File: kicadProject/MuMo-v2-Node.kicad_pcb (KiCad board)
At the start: 2 copper layers, 52 x 50.3 mm, 79 parts, among them Q1 PJC7400, SW1 Reset, U1 MCP73123T-22SI/MF, U2 LoRa-E5, U3 CP2102N-Axx-xQFN24, U4 eInk_Display_1.54"200x200px, U5 BME680, U6 TSL25911, U7 BR24G512FVT-5AE2, U8 BR24G512FVT-5AE2

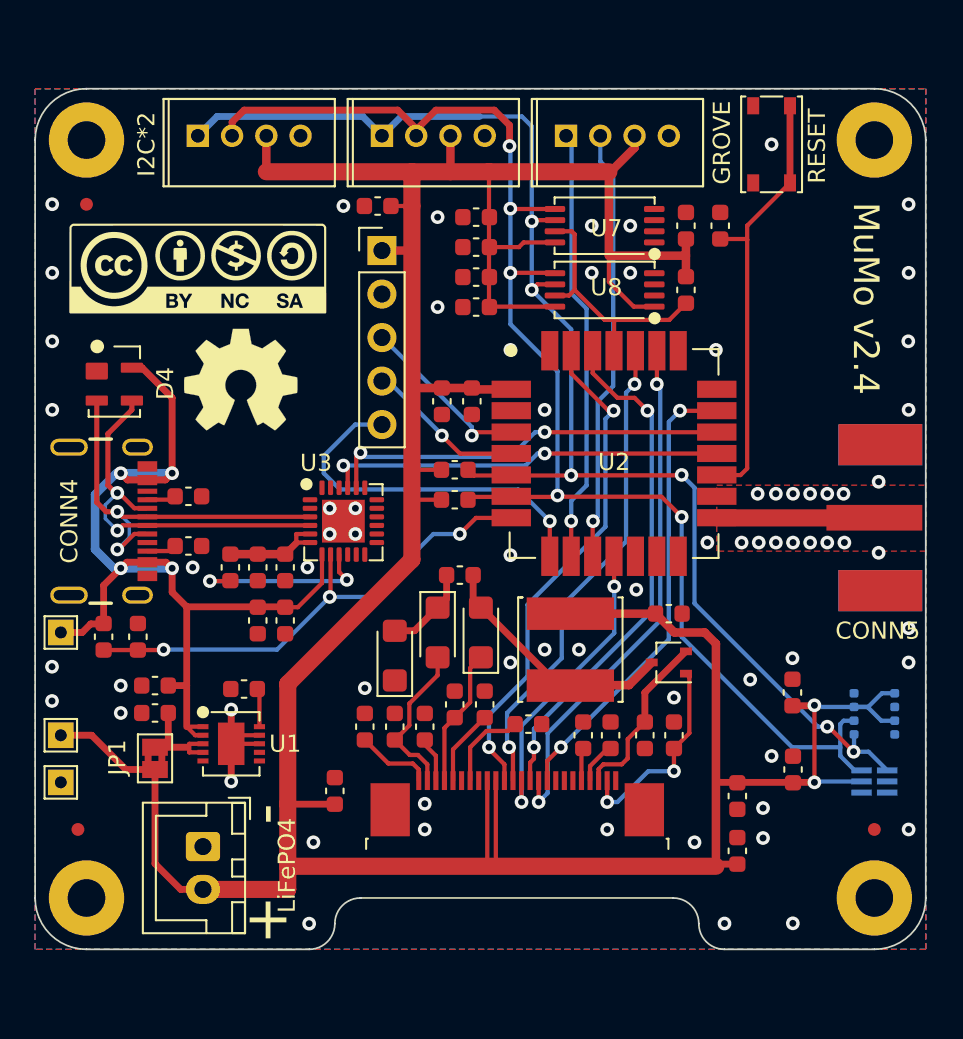
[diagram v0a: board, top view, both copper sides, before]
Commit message: add 3d model for enclosure
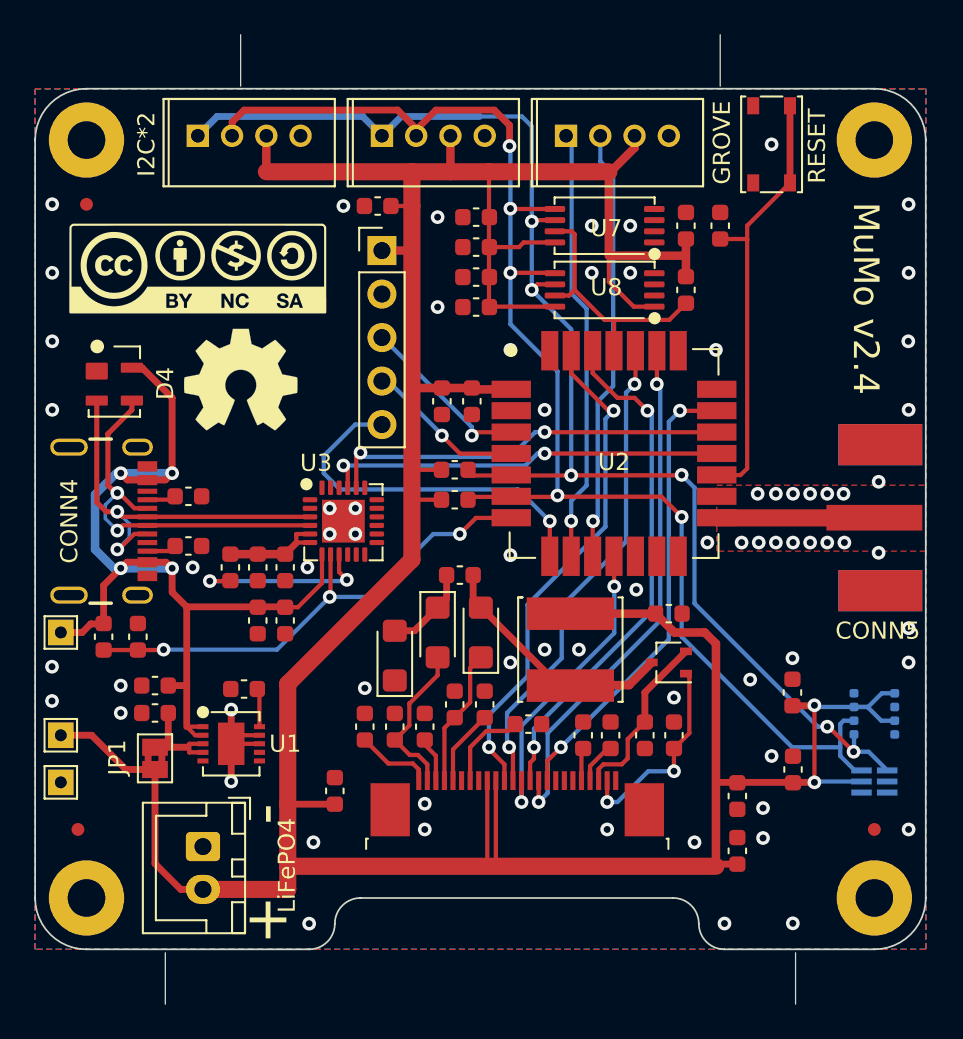
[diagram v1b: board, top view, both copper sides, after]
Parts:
- CONN2: value B2B-XH-A (LF)(SN) -> B2B-XH-A(LF)(SN)
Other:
- board size 52 x 50.3 mm -> 52 x 56.6 mm
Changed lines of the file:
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@@
     (property "DESCRIPTION" "JST XH 2pin THT Vertical")
     (property "MANUFACTURER" "JST")
-    (property "MPN" "B2B-XH-A (LF)(SN)")
+    (property "MPN" "B2B-XH-A(LF)(SN)")
     (property "Sheetfile" "MuMo-v2-Node.kicad_sch")
     (property "Sheetname" "")
+    (property "checked" "")
     (property "description" "JST XH 2pin THT Vertical")
     (property "has3Dmodel" "")
@@
     (property "remark" "LiFePO4 Battery")
     (property "stock" "1500000")
-    (property "supplier1Name" "Farnell")
-    (property "supplier1PartNumber" "1516276")
-    (property "supplier1PartURL" "https://be.farnell.com/jst-japan-solderless-terminals/b2b-xh-a-lf-sn/header-vertical-2way/dp/1516276")
+    (property "supplier1Name" "DigiKey")
+    (property "supplier1PartNumber" "455-2247-ND")
+    (property "supplier1PartURL" "https://www.digikey.be/nl/products/detail/jst-sales-america-inc/B2B-XH-A-LF-SN/1651045")
     (property "supplier2Name" "Digi-Key")
     (property "supplier2PartNumber" "455-2247-ND")
@@
         (effects (font (size 1 1) (thickness 0.15)))
     )
-    (fp_text value "B2B-XH-A (LF)(SN)" (at -3.75 4.75) (layer "F.Fab") hide
+    (fp_text value "B2B-XH-A(LF)(SN)" (at -3.75 4.75) (layer "F.Fab") hide
         (effects (font (size 1 1) (thickness 0.15)))
     )
@@
     (fp_circle (center 0 -6.44) (end 0.1 -6.44)
       (stroke (width 0.2) (type solid)) (fill none) (layer "F.Fab"))
-    (pad "1" smd rect (at 0 -2.8 90) (size 1.5 5.6) (layers "F.Cu" "F.Paste" "F.Mask")
+    (pad "1" smd rect (at 0 -2.8 90) (size 1.5 5.6) (layers "F.Cu" "F.Mask")
       (net 29 "Net-(CONN5-In)") (pinfunction "In") (pintype "passive"))
-    (pad "2" smd rect (at -4.26 -2.45 90) (size 2.4 4.9) (layers "F.Cu" "F.Paste" "F.Mask")
+    (pad "2" smd rect (at -4.26 -2.45 90) (size 2.4 4.9) (layers "F.Cu" "F.Mask")
       (net 1 "GND") (pinfunction "Ext") (pintype "passive"))
-    (pad "2" smd rect (at -4.26 -2.45 90) (size 2.4 4.9) (layers "B.Cu" "B.Paste" "B.Mask")
+    (pad "2" smd rect (at -4.26 -2.45 90) (size 2.4 4.9) (layers "B.Cu" "B.Mask")
       (net 1 "GND") (pinfunction "Ext") (pintype "passive"))
-    (pad "2" smd rect (at 4.26 -2.45 90) (size 2.4 4.9) (layers "F.Cu" "F.Paste" "F.Mask")
+    (pad "2" smd rect (at 4.26 -2.45 90) (size 2.4 4.9) (layers "F.Cu" "F.Mask")
       (net 1 "GND") (pinfunction "Ext") (pintype "passive"))
-    (pad "2" smd rect (at 4.26 -2.45 90) (size 2.4 4.9) (layers "B.Cu" "B.Paste" "B.Mask")
+    (pad "2" smd rect (at 4.26 -2.45 90) (size 2.4 4.9) (layers "B.Cu" "B.Mask")
       (net 1 "GND") (pinfunction "Ext") (pintype "passive"))
     (model "${KIPRJMOD}/libraries/inputs/CONSMA020.062-G--3DModel-STEP-269445.STEP"
@@
   (gr_arc (start 146.0308 107.808) (mid 143.90948 106.92932) (end 143.0308 104.808)
     (stroke (width 0.1) (type solid)) (layer "Edge.Cuts"))
+  (gr_line (start 155.0308 57.408) (end 155.0308 54.408)
+    (stroke (width 0.05588) (type default)) (layer "Edge.Cuts"))
   (gr_arc (start 143.0308 60.558) (mid 143.90948 58.43668) (end 146.0308 57.558)
     (stroke (width 0.1) (type solid)) (layer "Edge.Cuts"))
@@
   (gr_arc (start 180.2808 104.808) (mid 181.34146 105.24734) (end 181.7808 106.308)
     (stroke (width 0.1) (type solid)) (layer "Edge.Cuts"))
+  (gr_line (start 183.0308 57.408) (end 183.0308 54.408)
+    (stroke (width 0.05588) (type default)) (layer "Edge.Cuts"))
   (gr_arc (start 195.0308 104.808) (mid 194.15212 106.92932) (end 192.0308 107.808)
     (stroke (width 0.1) (type solid)) (layer "Edge.Cuts"))
@@
   (gr_arc (start 160.5308 106.308) (mid 160.09146 107.36866) (end 159.0308 107.808)
     (stroke (width 0.1) (type solid)) (layer "Edge.Cuts"))
+  (gr_line (start 150.6308 108.008) (end 150.6308 111.008)
+    (stroke (width 0.05588) (type default)) (layer "Edge.Cuts"))
+  (gr_line (start 187.4308 108.008) (end 187.4308 111.008)
+    (stroke (width 0.05588) (type default)) (layer "Edge.Cuts"))
   (gr_arc (start 160.5308 106.308) (mid 160.97014 105.24734) (end 162.0308 104.808)
     (stroke (width 0.1) (type solid)) (layer "Edge.Cuts"))
@@
   (gr_line locked (start 142.748 82.677) (end 220.726 82.677)
     (stroke (width 0.1) (type solid)) (layer "F.Fab"))
-  (gr_rect (start 142.748 57.658) (end 205.486 107.696)
+  (gr_rect (start 141.948 57.558) (end 204.636 107.796)
     (stroke (width 0.1) (type solid)) (fill none) (layer "F.Fab"))
   (gr_text "https://github.com/Strooom/MuMo-V2-Node-PCB" (at 168.7808 62.308) (layer "B.SilkS")
